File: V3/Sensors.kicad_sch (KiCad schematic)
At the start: 13 parts

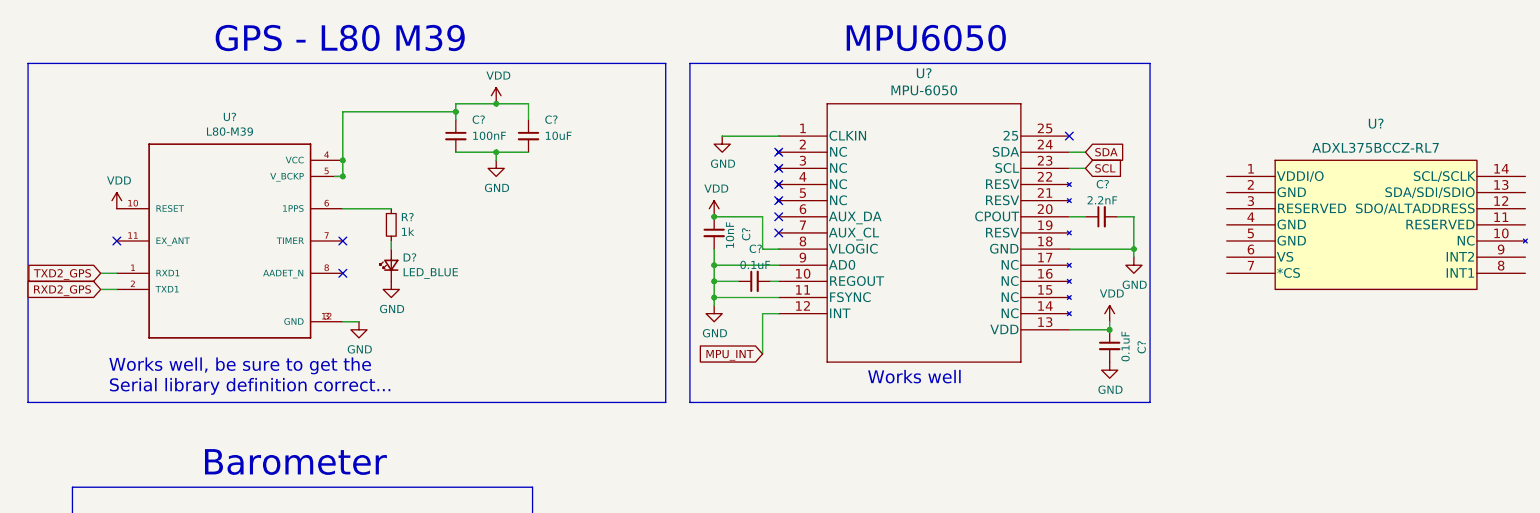
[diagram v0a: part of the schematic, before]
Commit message: Changed imu added flash chip
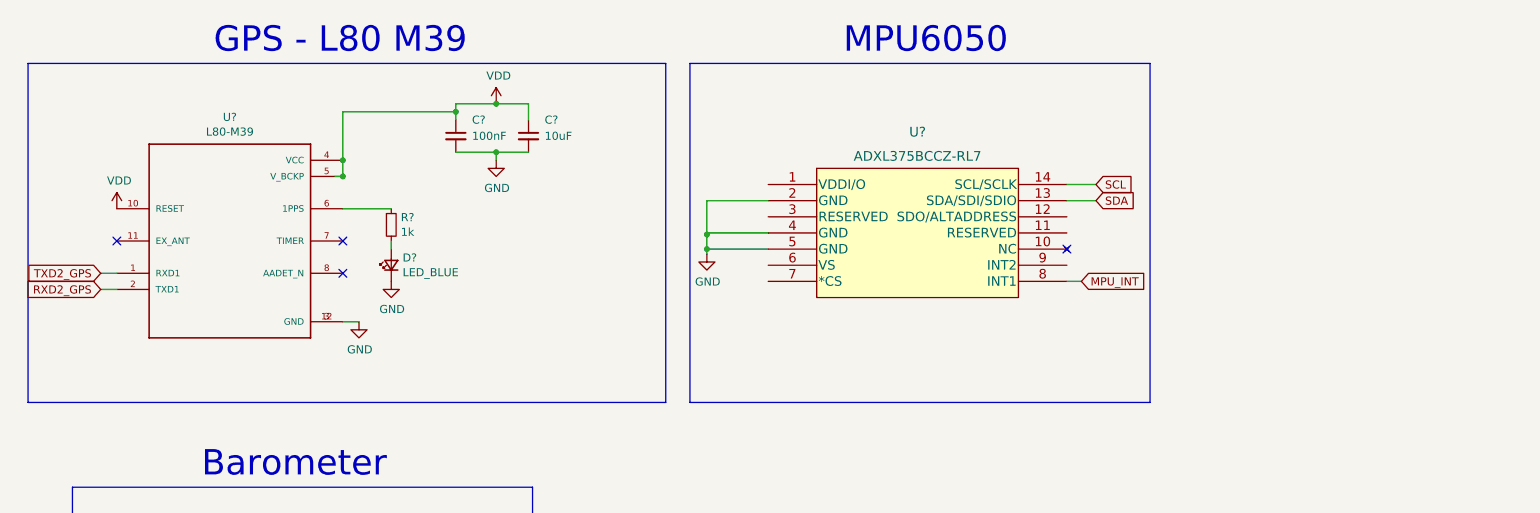
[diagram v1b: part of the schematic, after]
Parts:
- removed C? (x2): 0.1uF, Capacitor_SMD:C_0603_1608Metric, symbol Device:C_Small
- removed C?: 10nF, Capacitor_SMD:C_0603_1608Metric, symbol Device:C_Small
- removed C?: 2.2nF, Capacitor_SMD:C_0603_1608Metric, symbol Device:C_Small
- removed U?: MPU-6050, footprints:MPU-6050, symbol MPU-6050:MPU-6050
- U?: LCSC# (none) -> C481898
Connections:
- net GND: now also U?.2 (GND), U?.4 (GND), U?.5 (GND)
- net MPU_INT: now also U?.8 (INT1)
- net SCL: now also U?.14 (SCL/SCLK)
- net SDA: now also U?.13 (SDA/SDI/SDIO)
- no-connect marks 11 -> 5
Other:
- note removed: "Works well"
- note removed: "Works well, be sure to get the Serial library definition correct..."
- moved on the sheet: U?

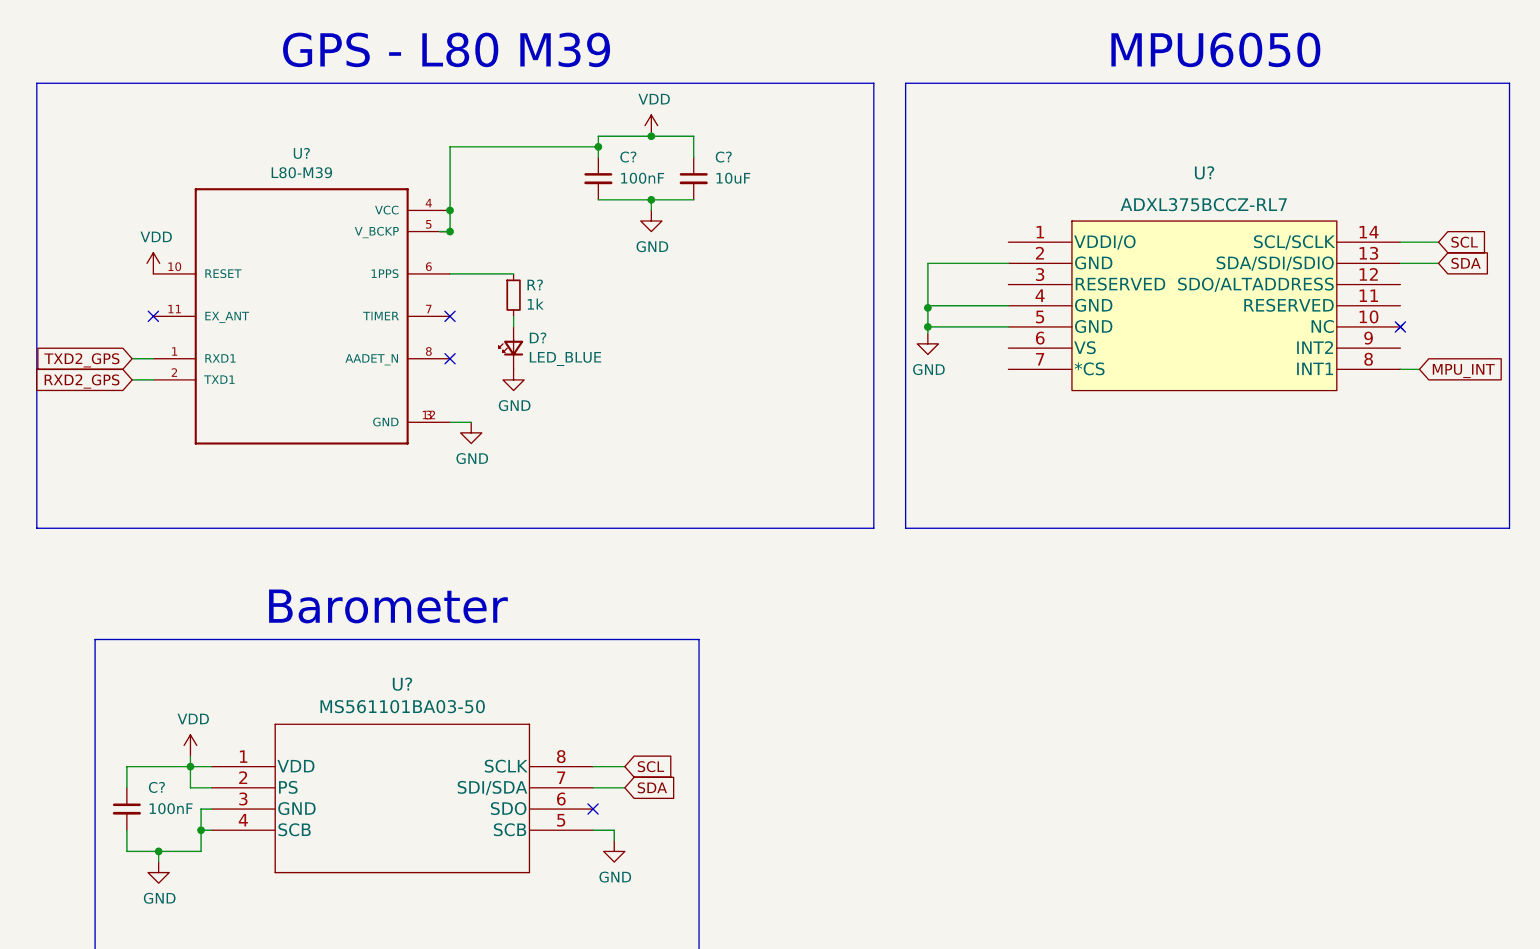
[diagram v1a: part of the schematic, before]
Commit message: Added sims, updated V3 board
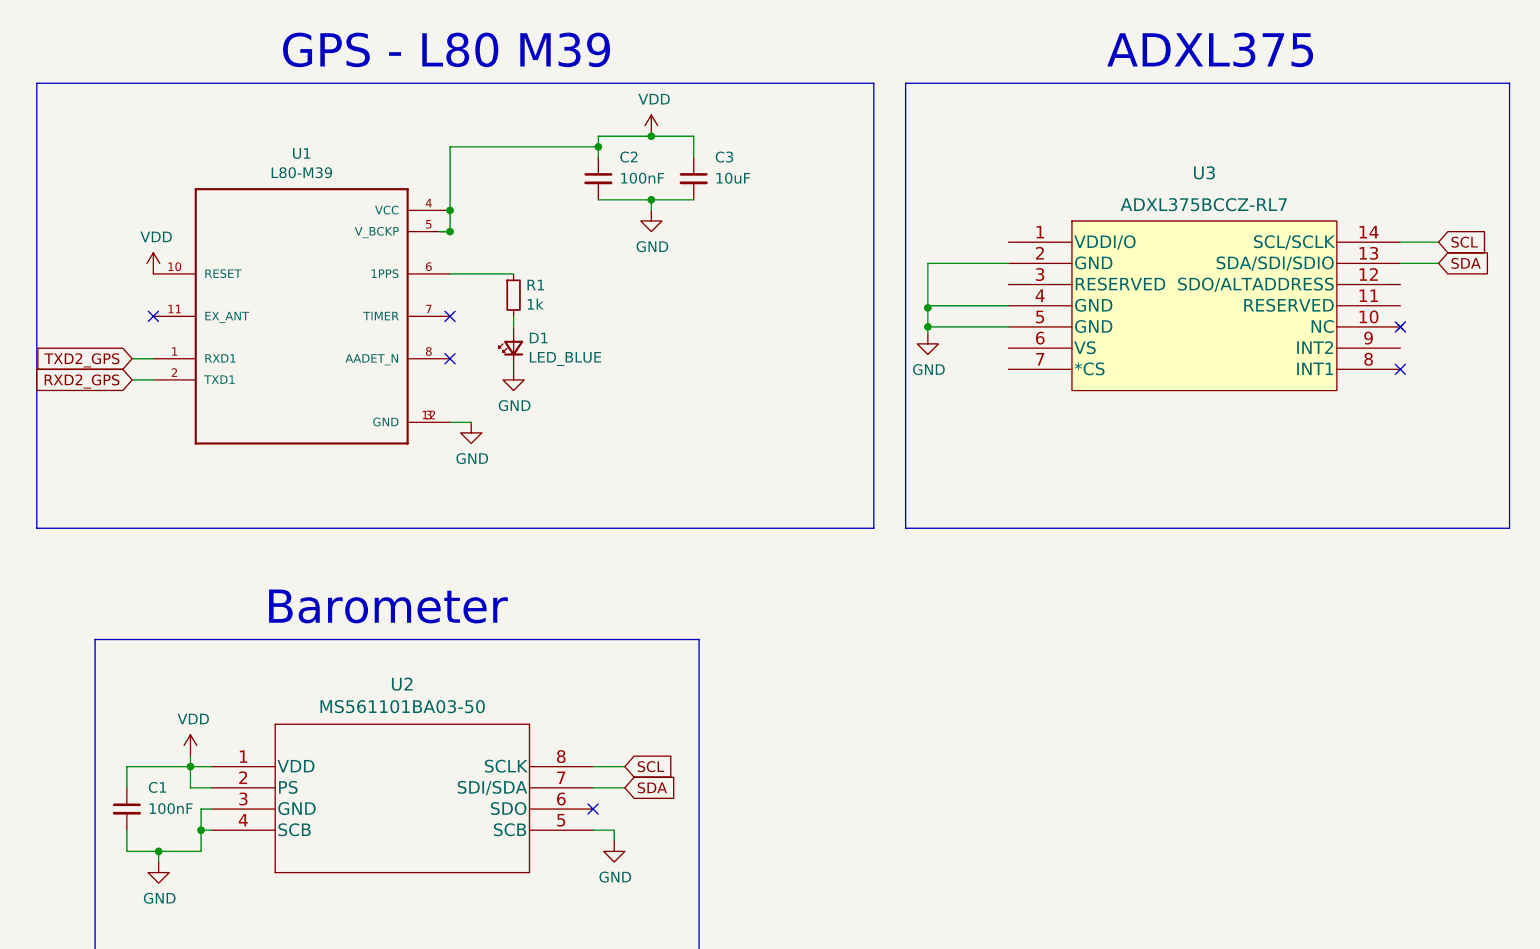
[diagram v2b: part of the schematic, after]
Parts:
- U1: renamed from U?; footprint XCVR_L80-M39:XCVR_L80-M39 -> Local_footprints:L80-M39
- U2: renamed from U?; footprint footprints:MS561101BA03-50 -> Local_footprints:MS561101BA03-50
- U3: renamed from U?; footprint LGA_CC-14-1_ADI -> Local_footprints:ADXL375BCCZ-RL7
- gave numbers to parts that had none: 5
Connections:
- net MPU_INT: no longer names the net of U3.8 (INT1)
- no-connect marks 5 -> 6
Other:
- note added: "ADXL375"
- note removed: "MPU6050"
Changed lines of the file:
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@@
   (no_connect (at 107.95 126.365))
   (no_connect (at 90.805 72.39))
+  (no_connect (at 204.724 73.66))
   (no_connect (at 90.805 67.31))
   (no_connect (at 204.724 68.58))
@@
     (stroke (width 0) (type default) (color 0 0 0 0))
   )
-  (wire (pts (xy 204.724 73.66) (xy 207.01 73.66))
-    (stroke (width 0) (type default) (color 0 0 0 0))
-  )
   (wire (pts (xy 108.585 53.34) (xy 114.935 53.34))
     (stroke (width 0) (type default) (color 0 0 0 0))
@@
     (stroke (width 0) (type default) (color 0 0 0 0))
   )
-  (text "MPU6050" (at 169.545 38.1 0)
+  (text "ADXL375" (at 169.545 38.1 0)
     (effects (font (size 3.9878 3.9878)) (justify left bottom))
   )
@@
     )
   )
-  (global_label "MPU_INT" (shape input) (at 207.01 73.66 0) (fields_autoplaced)
-    (effects (font (size 1.27 1.27)) (justify left))
-    (property "Intersheet References" "${INTERSHEET_REFS}" (id 0) (at 529.59 162.56 0)
-      (effects (font (size 1.27 1.27)) hide)
-    )
-  )
   (global_label "RXD2_GPS" (shape input) (at 52.705 74.93 180) (fields_autoplaced)
     (effects (font (size 1.27 1.27)) (justify right))
@@
   (symbol (lib_id "Device:C_Small") (at 120.015 50.8 0) (unit 1)
     (in_bom yes) (on_board yes)
-    (property "Reference" "C?" (id 0) (at 122.555 48.26 0)
+    (property "Reference" "C3" (id 0) (at 122.555 48.26 0)
       (effects (font (size 1.27 1.27)) (justify left))
     )
@@
   (symbol (lib_id "MS561101BA03-50:MS561101BA03-50") (at 85.09 126.365 0) (unit 1)
     (in_bom yes) (on_board yes)
-    (property "Reference" "U?" (id 0) (at 85.09 111.4552 0)
+    (property "Reference" "U2" (id 0) (at 85.09 111.4552 0)
       (effects (font (size 1.524 1.524)))
     )
@@
       (effects (font (size 1.524 1.524)))
     )
-    (property "Footprint" "footprints:MS561101BA03-50" (id 2) (at 85.09 115.189 0)
+    (property "Footprint" "Local_footprints:MS561101BA03-50" (id 2) (at 85.09 115.189 0)
       (effects (font (size 1.524 1.524)) hide)
     )
@@
   (symbol (lib_id "Device:R_Small") (at 98.425 64.77 0) (unit 1)
     (in_bom yes) (on_board yes)
-    (property "Reference" "R?" (id 0) (at 99.9236 63.6016 0)
+    (property "Reference" "R1" (id 0) (at 99.9236 63.6016 0)
       (effects (font (size 1.27 1.27)) (justify left))
     )
@@
   (symbol (lib_id "power:GND") (at 93.345 80.01 0) (unit 1)
     (in_bom yes) (on_board yes)
-    (property "Reference" "#PWR?" (id 0) (at 93.345 86.36 0)
+    (property "Reference" "#PWR0105" (id 0) (at 93.345 86.36 0)
       (effects (font (size 1.27 1.27)) hide)
     )
@@
   (symbol (lib_id "power:GND") (at 114.935 54.61 0) (unit 1)
     (in_bom yes) (on_board yes)
-    (property "Reference" "#PWR?" (id 0) (at 114.935 60.96 0)
+    (property "Reference" "#PWR0108" (id 0) (at 114.935 60.96 0)
       (effects (font (size 1.27 1.27)) hide)
     )
@@
   (symbol (lib_id "power:GND") (at 148.082 69.342 0) (unit 1)
     (in_bom yes) (on_board yes)
-    (property "Reference" "#PWR?" (id 0) (at 148.082 75.692 0)
+    (property "Reference" "#PWR0101" (id 0) (at 148.082 75.692 0)
       (effects (font (size 1.27 1.27)) hide)
     )
@@
   (symbol (lib_id "L2_board-rescue:L80-M39-L80-M39") (at 73.025 67.31 0) (unit 1)
     (in_bom yes) (on_board yes)
-    (property "Reference" "U?" (id 0) (at 73.025 47.8282 0))
+    (property "Reference" "U1" (id 0) (at 73.025 47.8282 0))
     (property "Value" "L80-M39" (id 1) (at 73.025 50.1396 0))
-    (property "Footprint" "XCVR_L80-M39:XCVR_L80-M39" (id 2) (at 73.025 67.31 0)
+    (property "Footprint" "Local_footprints:L80-M39" (id 2) (at 73.025 67.31 0)
       (effects (font (size 1.27 1.27)) (justify left bottom) hide)
     )
@@
   (symbol (lib_id "Device:C_Small") (at 52.07 126.365 0) (unit 1)
     (in_bom yes) (on_board yes)
-    (property "Reference" "C?" (id 0) (at 54.61 123.825 0)
+    (property "Reference" "C1" (id 0) (at 54.61 123.825 0)
       (effects (font (size 1.27 1.27)) (justify left))
     )
@@
   (symbol (lib_id "power:GND") (at 55.88 132.715 0) (unit 1)
     (in_bom yes) (on_board yes)
-    (property "Reference" "#PWR?" (id 0) (at 55.88 139.065 0)
+    (property "Reference" "#PWR0103" (id 0) (at 55.88 139.065 0)
       (effects (font (size 1.27 1.27)) hide)
     )
@@
   (symbol (lib_id "power:VDD") (at 55.245 62.23 0) (unit 1)
     (in_bom yes) (on_board yes)
-    (property "Reference" "#PWR?" (id 0) (at 55.245 66.04 0)
+    (property "Reference" "#PWR0107" (id 0) (at 55.245 66.04 0)
       (effects (font (size 1.27 1.27)) hide)
     )
@@
   (symbol (lib_id "power:GND") (at 98.425 73.66 0) (unit 1)
     (in_bom yes) (on_board yes)
-    (property "Reference" "#PWR?" (id 0) (at 98.425 80.01 0)
+    (property "Reference" "#PWR0106" (id 0) (at 98.425 80.01 0)
       (effects (font (size 1.27 1.27)) hide)
     )
@@
   (symbol (lib_id "ADXL375BCCZ-RL7:ADXL375BCCZ-RL7") (at 141.224 58.42 0) (unit 1)
     (in_bom yes) (on_board yes) (fields_autoplaced)
-    (property "Reference" "U?" (id 0) (at 181.229 50.165 0)
+    (property "Reference" "U3" (id 0) (at 181.229 50.165 0)
       (effects (font (size 1.524 1.524)))
     )
@@
       (effects (font (size 1.524 1.524)))
     )
-    (property "Footprint" "LGA_CC-14-1_ADI" (id 2) (at 176.784 52.324 0)
+    (property "Footprint" "Local_footprints:ADXL375BCCZ-RL7" (id 2) (at 176.784 52.324 0)
       (effects (font (size 1.524 1.524)) hide)
     )
@@
   (symbol (lib_id "power:VDD") (at 59.69 120.015 0) (unit 1)
     (in_bom yes) (on_board yes)
-    (property "Reference" "#PWR?" (id 0) (at 59.69 123.825 0)
+    (property "Reference" "#PWR0102" (id 0) (at 59.69 123.825 0)
       (effects (font (size 1.27 1.27)) hide)
     )
@@
   (symbol (lib_id "power:GND") (at 110.49 130.175 0) (unit 1)
     (in_bom yes) (on_board yes)
-    (property "Reference" "#PWR?" (id 0) (at 110.49 136.525 0)
+    (property "Reference" "#PWR0104" (id 0) (at 110.49 136.525 0)
       (effects (font (size 1.27 1.27)) hide)
     )
@@
   (symbol (lib_id "power:VDD") (at 114.935 45.72 0) (unit 1)
     (in_bom yes) (on_board yes)
-    (property "Reference" "#PWR?" (id 0) (at 114.935 49.53 0)
+    (property "Reference" "#PWR0109" (id 0) (at 114.935 49.53 0)
       (effects (font (size 1.27 1.27)) hide)
     )
@@
   (symbol (lib_id "Device:C_Small") (at 108.585 50.8 0) (unit 1)
     (in_bom yes) (on_board yes)
-    (property "Reference" "C?" (id 0) (at 111.125 48.26 0)
+    (property "Reference" "C2" (id 0) (at 111.125 48.26 0)
       (effects (font (size 1.27 1.27)) (justify left))
     )
@@
   (symbol (lib_id "Device:LED_Small") (at 98.425 71.12 90) (unit 1)
     (in_bom yes) (on_board yes)
-    (property "Reference" "D?" (id 0) (at 100.203 69.9516 90)
+    (property "Reference" "D1" (id 0) (at 100.203 69.9516 90)
       (effects (font (size 1.27 1.27)) (justify right))
     )

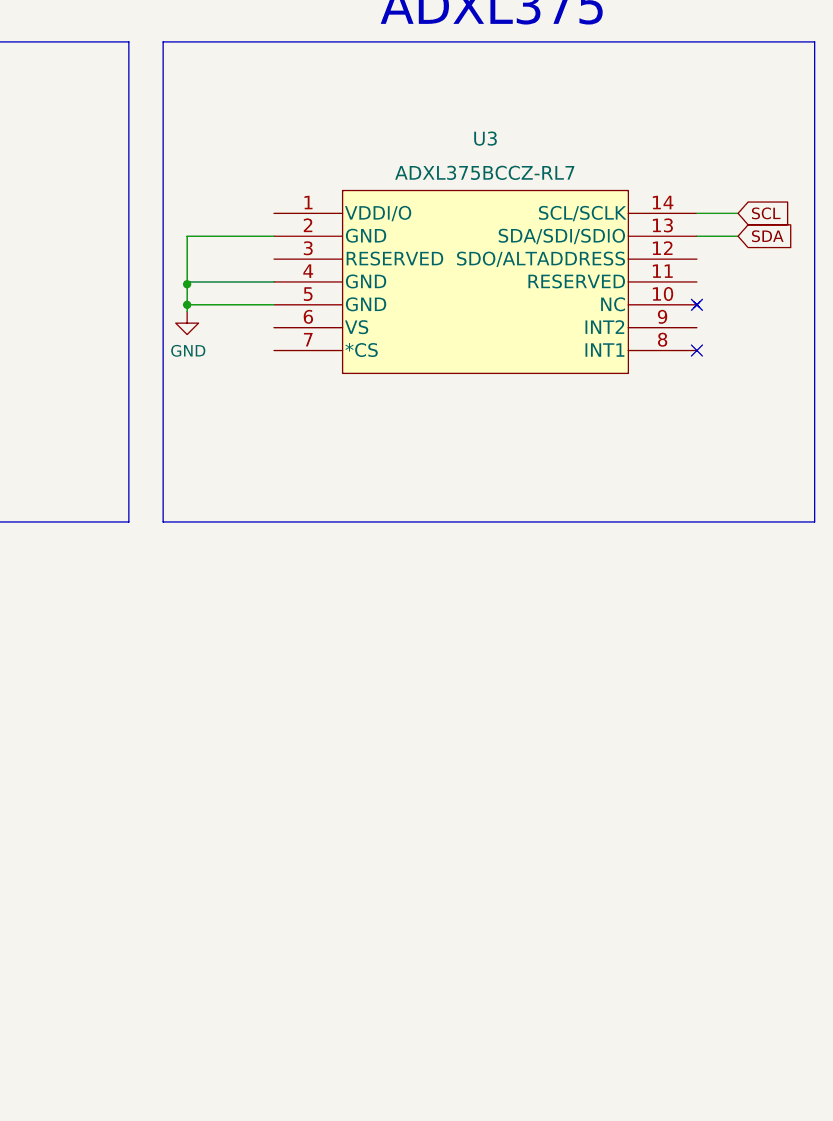
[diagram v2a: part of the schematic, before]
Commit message: Added mpu6050 back
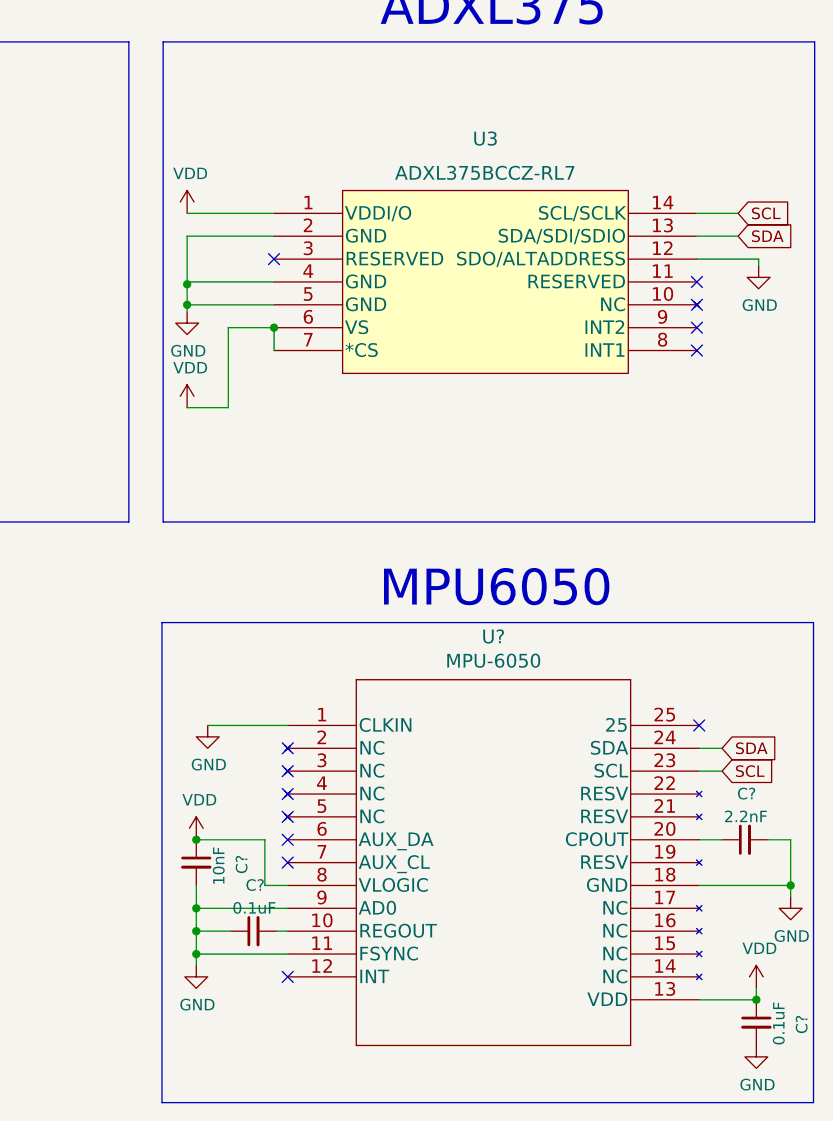
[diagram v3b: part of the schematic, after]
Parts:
- added C?: 10nF, Capacitor_SMD:C_0603_1608Metric, symbol Device:C_Small
- added C? (x2): 0.1uF, Capacitor_SMD:C_0603_1608Metric, symbol Device:C_Small
- added C?: 2.2nF, Capacitor_SMD:C_0603_1608Metric, symbol Device:C_Small
- added U?: MPU-6050, Local_footprints:MPU-6050, symbol MPU-6050:MPU-6050
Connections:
- net GND: now also U3.12 (SDO/ALTADDRESS), C?.1, C?.2, C?.2, C?.2, U?.1 (CLKIN), U?.11 (FSYNC), U?.18 (GND), U?.9 (AD0)
- net SCL: now also U?.23 (SCL)
- net SDA: now also U?.24 (SDA)
- net VDD: now also U3.1 (VDDI/O), U3.6 (VS), U3.7 (*CS), C?.1, C?.1, U?.13 (VDD), U?.8 (VLOGIC)
- new net: C?.2, U?.10 (REGOUT)
- new net: C?.1, U?.20 (CPOUT)
- no-connect marks 6 -> 17
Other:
- note added: "MPU6050"
